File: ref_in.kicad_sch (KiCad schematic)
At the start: 15 parts, among them U1101 74LVC2GU04, U1102 74LVC2G04

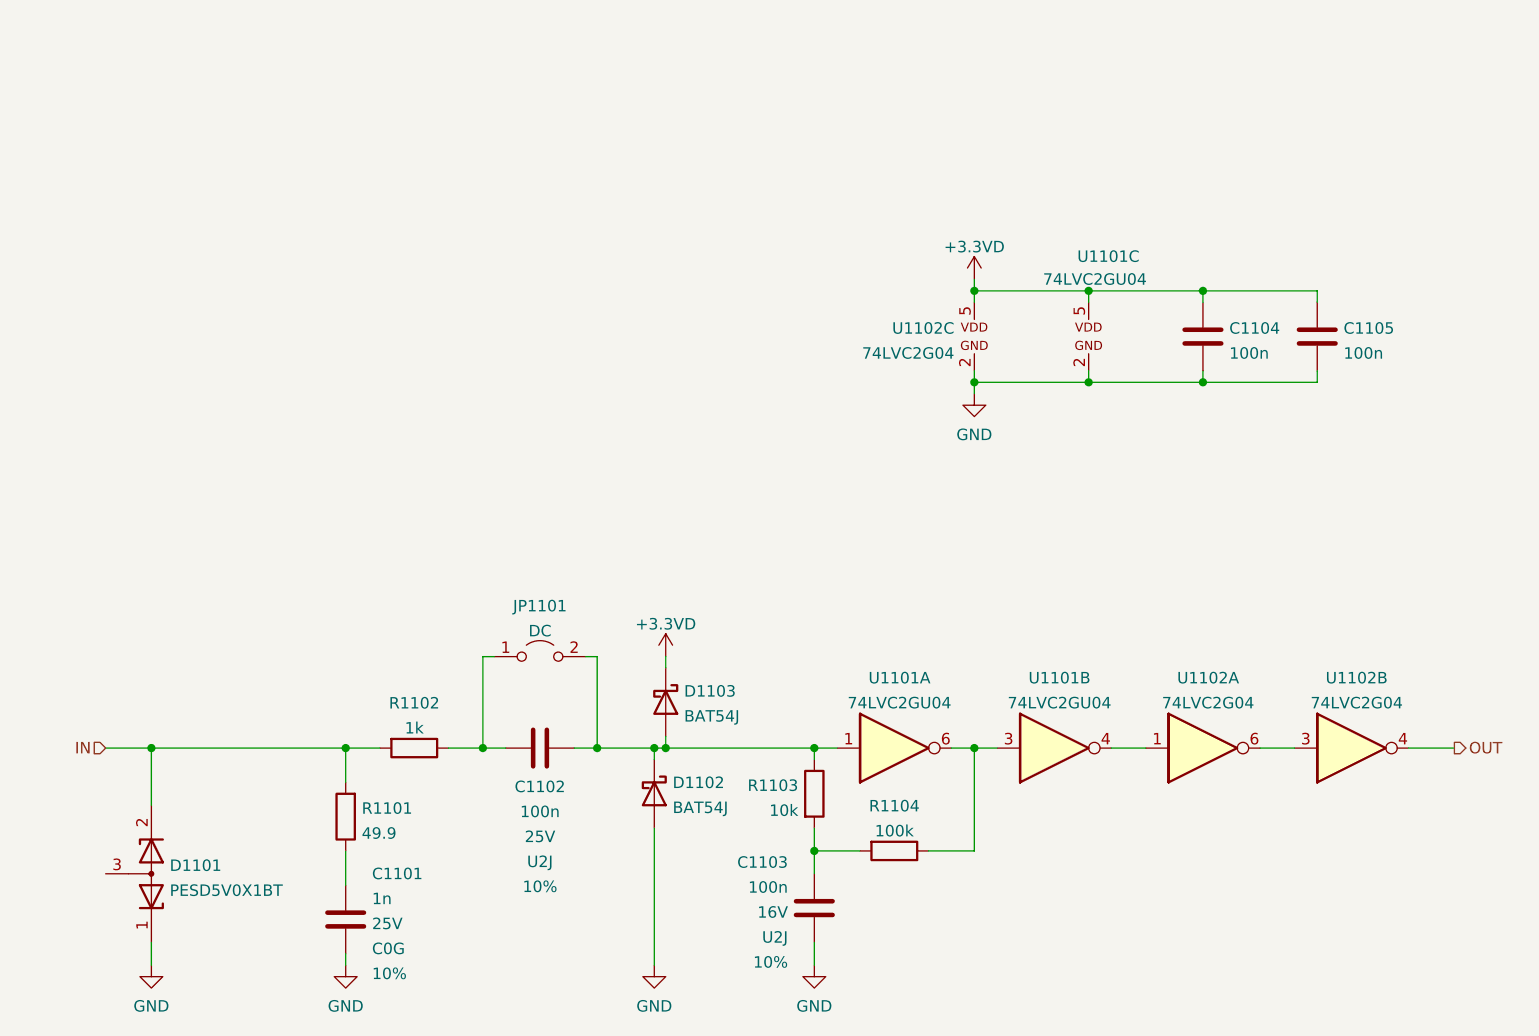
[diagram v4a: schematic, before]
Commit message: Schematic: better LDO output capacitor selection, clarified BOM
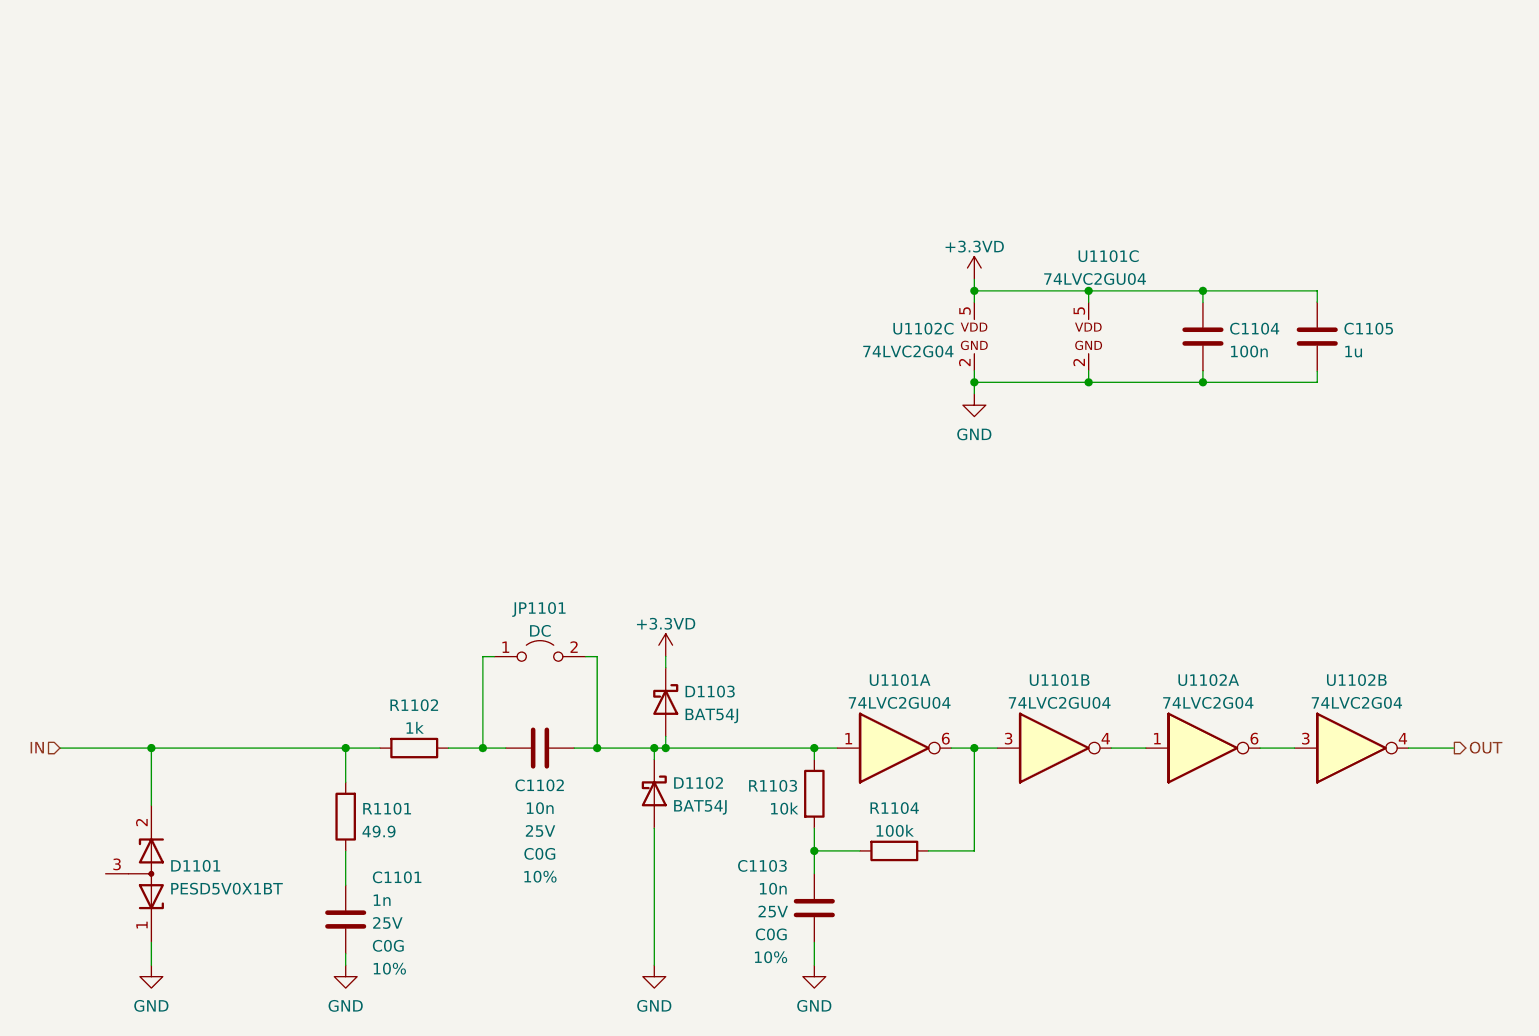
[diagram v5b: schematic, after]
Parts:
- C1102: value 100n -> 10n; footprint Capacitor_SMD:C_1206_3216Metric -> Capacitor_SMD:C_0805_2012Metric; Spec2 U2J -> C0G
- C1103: value 100n -> 10n; footprint Capacitor_SMD:C_1206_3216Metric -> Capacitor_SMD:C_0805_2012Metric; Spec1 16V -> 25V; Spec2 U2J -> C0G
- C1104: Spec1 16V -> (none); Spec2 X5R -> (none); Tolerance 20% -> (none)
- C1105: value 100n -> 1u; Spec1 16V -> (none); Spec2 X5R -> (none); Tolerance 20% -> (none)

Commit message: Schematic: yet another update -Improve way caps are specified once again -Update cap voltages based on ESD simulation -Make anti-aliasing LC filter more practical - with much less inductors -Specify Mfr & MfrPN for almost all components (most from Mouser, some from Digikey)
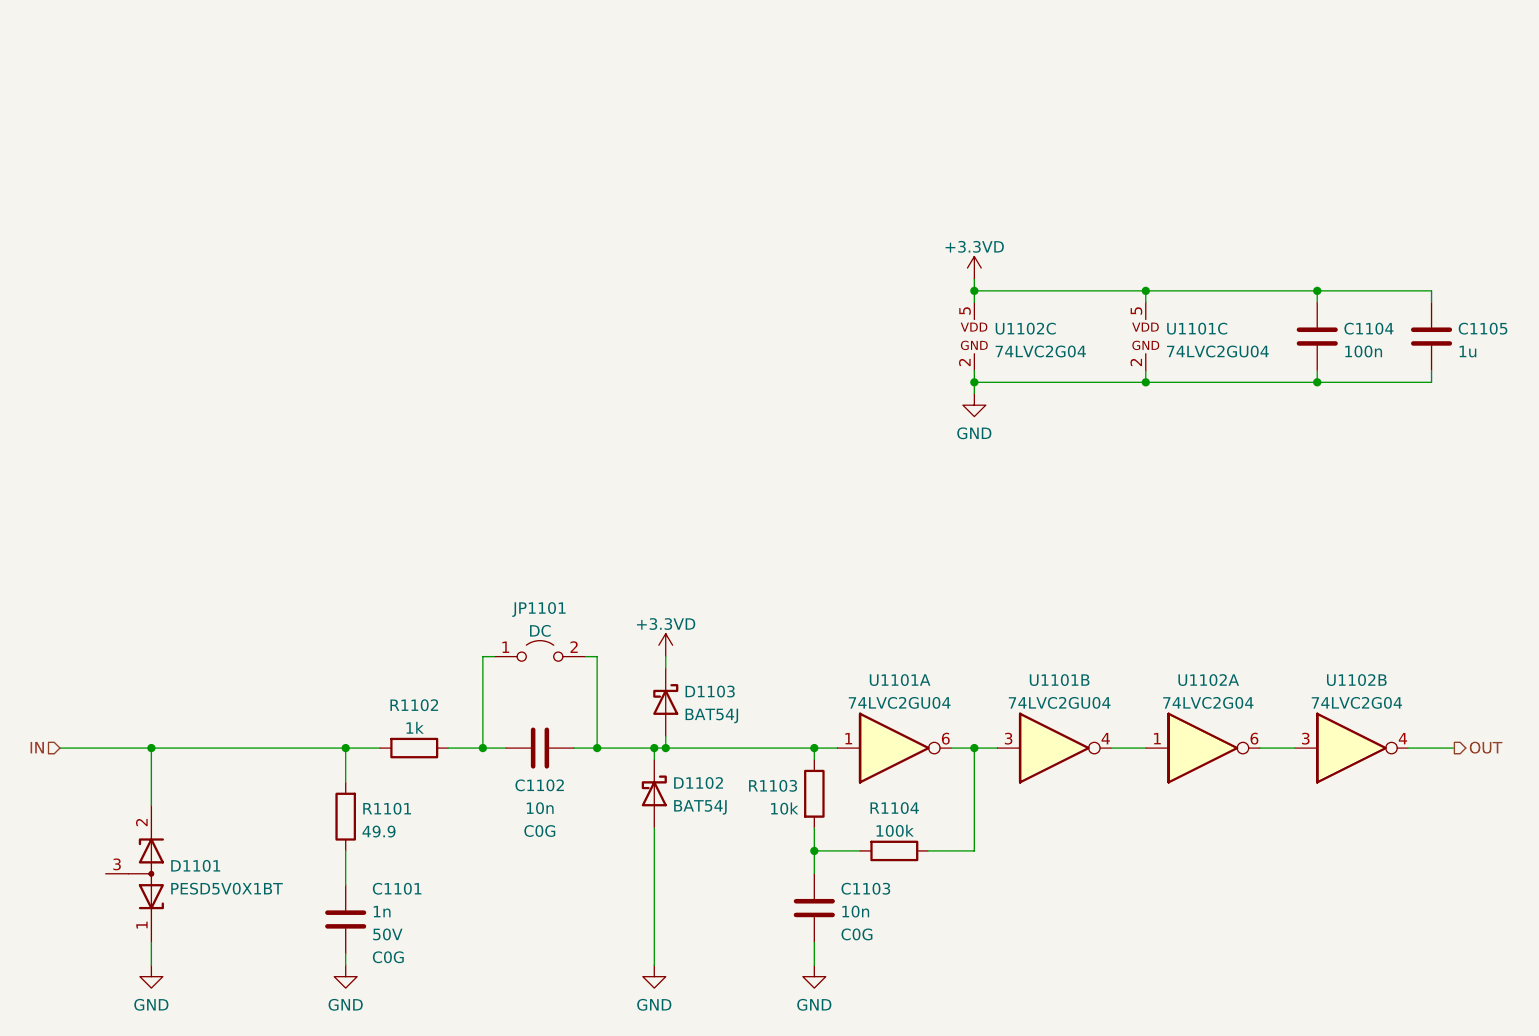
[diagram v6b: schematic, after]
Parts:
- C1101: Mfr (none) -> KEMET; Mfr PN (none) -> C0805C102J5GAC; Spec1 25V -> 50V; Tolerance 10% -> (none)
- C1102, C1103: Mfr (none) -> Murata; Mfr PN (none) -> GRM2165C2A103JA01; Spec1 25V -> (none); Tolerance 10% -> (none)
- C1104: Mfr (none) -> Samsung; Mfr PN (none) -> CL21B104KBFNNNE
- C1105: Mfr (none) -> Samsung; Mfr PN (none) -> CL21B105KOFNNNG
- D1101: Mfr (none) -> Nexperia; Mfr PN (none) -> PESD5V0X1BT,215
- D1102, D1103: footprint Diode_SMD:D_SOD-323F -> Diode_SMD:D_SOD-323_HandSoldering; Mfr (none) -> Nexperia; Mfr PN (none) -> BAT54HGWX
- R1101, R1102, R1103, R1104: Tolerance 5% -> (none)
- U1101: Mfr (none) -> Texas Instruments; Mfr PN (none) -> 74LVC2GU04DBVRG4
- U1102: Mfr (none) -> Nexperia; Mfr PN (none) -> 74LVC2G04GV-Q100H
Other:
- moved on the sheet: C1104, C1105, U1101C

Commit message: Schematic: add PNs for resistors
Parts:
- R1101: Mfr (none) -> Bourns; Mfr PN (none) -> CR0805-FX-49R9ELF
- R1102: Mfr (none) -> Bourns; Mfr PN (none) -> CR0805-FX-1001ELF
- R1103: Mfr (none) -> Bourns; Mfr PN (none) -> CR0805-FX-1002ELF
- R1104: Mfr (none) -> Bourns; Mfr PN (none) -> CR0805-FX-1003ELF
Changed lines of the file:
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@@
+      (effects (font (size 1.27 1.27)) hide)
+    )
+    (property "Mfr" "Bourns" (id 5) (at 95.25 109.22 0)
+      (effects (font (size 1.27 1.27)) hide)
+    )
+    (property "Mfr PN" "CR0805-FX-49R9ELF" (id 6) (at 95.25 109.22 0)
       (effects (font (size 1.27 1.27)) hide)
     )
@@
       (effects (font (size 1.27 1.27)) hide)
     )
+    (property "Mfr" "Bourns" (id 5) (at 156.21 113.03 0)
+      (effects (font (size 1.27 1.27)) hide)
+    )
+    (property "Mfr PN" "CR0805-FX-1003ELF" (id 6) (at 156.21 113.03 0)
+      (effects (font (size 1.27 1.27)) hide)
+    )
     (pin "1")
     (pin "2")
@@
       (effects (font (size 1.27 1.27)) hide)
     )
+    (property "Mfr" "Bourns" (id 5) (at 102.87 101.6 0)
+      (effects (font (size 1.27 1.27)) hide)
+    )
+    (property "Mfr PN" "CR0805-FX-1001ELF" (id 6) (at 102.87 101.6 0)
+      (effects (font (size 1.27 1.27)) hide)
+    )
     (pin "1")
     (pin "2")
@@
       (effects (font (size 1.27 1.27)) hide)
     )
+    (property "Mfr" "Bourns" (id 5) (at 147.32 106.68 0)
+      (effects (font (size 1.27 1.27)) hide)
+    )
+    (property "Mfr PN" "CR0805-FX-1002ELF" (id 6) (at 147.32 106.68 0)
+      (effects (font (size 1.27 1.27)) hide)
+    )
